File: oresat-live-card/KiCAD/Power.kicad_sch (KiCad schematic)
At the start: 112 parts, among them Q2 PMV45EN2R, Q3 DMP2240UDM, Q4 PMV45EN2R, Q5 DMP3050LVT-7, Q6 DMP3050LVT-7, U12 MIC842LYC5, U13 MIC842LYC5, U14 MAX4211FETE, U15 LTC3624-5, U16 MAX7310ATE, U21 TLV733P-Q1, U22 TS5A21366, U5 LTC3624-5

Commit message: Updated OreSat Live Card. Added changes from the C3 v6 Octavo circuitry and GPS card update. Fixed some GitHub issues. Board layout still in progress.
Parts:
- added C84, C85: CL05B104KO5NNNC, Resistor_SMD:R_0603_1608Metric, symbol Device:C_Small
- added R75: 10k, Resistor_SMD:R_0603_1608Metric, symbol oresat-passives:R-US
- added R95: 1k, Resistor_SMD:R_0603_1608Metric, symbol oresat-passives:R-US
- added TP28, TP31: TEST-POINT, oresat-misc:TestPoint_Pad_D1.0mm, symbol oresat-misc:Test-Point-1mm-round
- D12, D6, D7, D8, D9: symbol oresat-live-card-eagle-import:LED-GREEN0603 -> Device:LED
- Q2, Q4: symbol oresat-live-card-eagle-import:PMV45EN -> Device:Q_NMOS_GSD
- Q3: symbol oresat-live-card-eagle-import:MOSFET-PCH-SOT23-6 -> oresat-transistors:DMP2240UDM-7
- Q5, Q6: footprint oresat-live-card:SOT23-6 -> Package_TO_SOT_SMD:SOT-23-6; symbol oresat-live-card-eagle-import:MOSFET-PCH-SOT23-6 -> oresat-transistors:DMP3050LVT-7
- R20, R22: value 4.7k -> 10k; symbol oresat-live-card-eagle-import:R-US_0603-A -> oresat-passives:R-US
- R32, R33, R34, R35, R36, R37, R38, R39, R40, R41, R42, R43, R44, R45, R46, R47, R48, R49, R50, R51, R52, R53, R54, R55, R56, R57, R58, R59, R60, R61, R62, R64, R65, R66, R67, R68, R69, R70, R71, R72, R94: symbol oresat-live-card-eagle-import:R-US_0603-A -> oresat-passives:R-US
- R63: symbol oresat-live-card-eagle-import:R-US_R1206 -> oresat-passives:R-US
- R92, R93: value 1k -> 100; symbol oresat-live-card-eagle-import:R-US_0603-A -> oresat-passives:R-US
- TP19, TP23, TP24, TP26, TP41, TP42, TP43, TP44, TP45, TP47, TP52, TP53, TP54, TP55, TP57, TP63, TP64, TP67, TP68: footprint oresat-live-card:PAD.03X.04 -> oresat-misc:TestPoint_Pad_D1.0mm; symbol oresat-live-card-eagle-import:TEST-POINT -> oresat-misc:Test-Point-1mm-round
- U12, U13: symbol oresat-live-card-eagle-import:MIC842LYC5 -> oresat-ics:MIC842LYC5
- U14: symbol oresat-live-card-eagle-import:MAX4211 -> oresat-ics:MAX4211FETE
- U15, U5: symbol U-Linear Tech-LTC3624:LTC3624 -> oresat-ics:LTC3624
- U16: symbol oresat-live-card-eagle-import:MAX7310 -> oresat-ics:MAX7310
- U21: symbol U-TI-TLV73311PQDBVRQ1-Linear:TLV733P-Q1 -> oresat-ics:TLV733P-Q1
- U22: symbol U-TI-TS5A21366-2xSPST-analog-switch:TS5A21366 -> oresat-ics:TS5A21366
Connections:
- net CB_CTRL: now also R75.1; no longer Q5.1 (G), R64.1
- net GND: now also D12.1 (K), D6.1 (K), D7.1 (K), D8.1 (K), D9.1 (K), U14.17 (GND), U16.17 (GND); no longer D12.C, D6.C, D7.C, D8.C, D9.C, U14.EPAD (GND), U16.EPAD (GND)
- net VBUS: now also Q6.1 (D), Q6.2 (D), Q6.6 (D)
- net VBUSP: now also Q5.4 (S), C85.1; no longer Q5.6 (D)
- net at Q4.3 (D), R52.1: now also Q6.3 (G); no longer Q6.1 (G)
- net at R20.2: now also D8.2 (A); no longer D8.A
- net at Q5.5 (D), R63.2, R64.2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: now also Q5.1 (D), Q5.2 (D), Q5.6 (D), C84.2
- net at R61.1: now also D7.2 (A); no longer D7.A
- net at C44.1, R63.1, U14.16 (RS+): now also Q6.4 (S); no longer Q6.6 (D)
- net at R49.1: now also D6.2 (A); no longer D6.A
- net at U16.11 (IO6): now also TP31.1
- net at R22.2: now also D9.2 (A); no longer D9.A
- net at R62.2: now also D12.2 (A); no longer D12.A
- net BOOT0: no longer names the net of U16.10 (IO5)
- net BOOT0: now also TP28.1
- net PB6/SCL renamed SYSBOOT2
- net PB7/SDA: no longer names the net of TP68.1, U16.5 (IO1)
- new net: C85.2, R95.1
- new net: C84.1, Q5.3 (G), R64.1, R75.2, R95.2
- no-connect marks 3 -> 2
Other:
- note added: "Circuit breaker switch with ~10 ms soft start"
- note added: "IO0 is open-drain. Pull-up resistor and optional GND jumper on page 4"
- moved on the sheet: C16, C17, C20, C3, C32, C33, C34, C35, C36, C37, C38, C39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

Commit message: Finished layout, and cleaned up more errors/warnings
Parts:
- U15, U5: footprint oresat-footprints:DFN-8-1EP_3x3mm_P0.5mm_EP1.65x2.38mm_ThermalVias0.3mm -> oresat-ics:DFN-8-1EP_3x3mm_P0.5mm_EP1.65x2.38mm_ThermalVias0.3mm
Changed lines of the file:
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@@
       (effects (font (size 1.27 1.27)))
     )
-    (property "Footprint" "oresat-footprints:DFN-8-1EP_3x3mm_P0.5mm_EP1.65x2.38mm_ThermalVias0.3mm" (at 226.06 223.52 0)
+    (property "Footprint" "oresat-ics:DFN-8-1EP_3x3mm_P0.5mm_EP1.65x2.38mm_ThermalVias0.3mm" (at 226.06 223.52 0)
       (effects (font (size 1.27 1.27)) hide)
     )
@@
       (effects (font (size 1.27 1.27)))
     )
-    (property "Footprint" "oresat-footprints:DFN-8-1EP_3x3mm_P0.5mm_EP1.65x2.38mm_ThermalVias0.3mm" (at 344.17 223.52 0)
-      (effects (font (size 1.27 1.27)) hide)
-    )
+    (property "Footprint" "oresat-ics:DFN-8-1EP_3x3mm_P0.5mm_EP1.65x2.38mm_ThermalVias0.3mm" (at 344.17 223.52 0)
+      (effects (font (size 1.27 1.27)) hide)
+    )

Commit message: Updated silk screen and small schematic changes
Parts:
- TP55: footprint oresat-misc:TestPoint_Pad_D1.0mm -> oresat-misc:TestPoint-0.75mm-th
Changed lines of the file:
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@@
       (effects (font (size 1.27 1.27)) hide)
     )
-    (property "Footprint" "oresat-misc:TestPoint_Pad_D1.0mm" (at 407.67 30.48 0)
+    (property "Footprint" "oresat-misc:TestPoint-0.75mm-th" (at 407.67 30.48 0)
       (effects (font (size 1.27 1.27)) hide)
     )

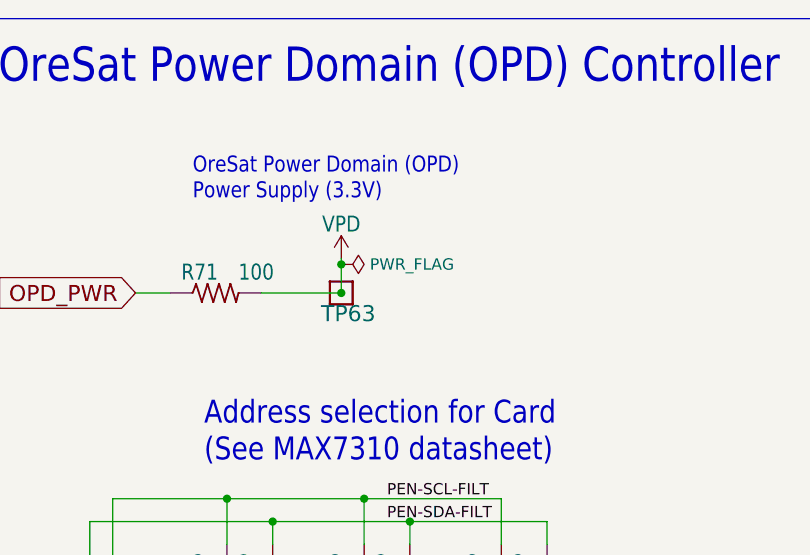
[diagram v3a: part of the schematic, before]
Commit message: Fixed issue with VPD diodes
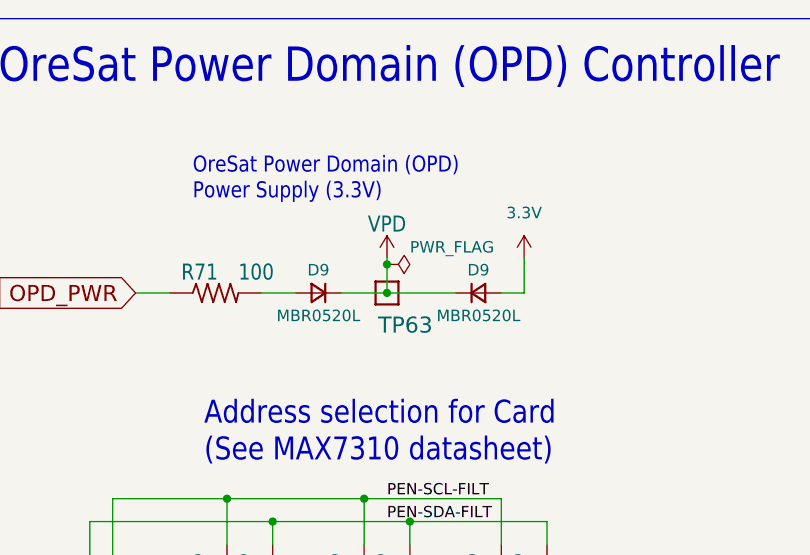
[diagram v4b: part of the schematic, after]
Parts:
- added D9 (x2): MBR0520L, Diode_SMD:D_SOD-123, symbol Device:D_Small
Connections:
- net VPD: now also D9.1 (K), D9.1 (K); no longer R71.2
- new net: D9.2 (A), R71.2
- new net 3.3V: D9.2 (A)
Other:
- moved on the sheet: TP63
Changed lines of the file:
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@@
   (junction (at 266.7 218.44) (diameter 0) (color 0 0 0 0)
   )
-  (junction (at 73.66 48.26) (diameter 0) (color 0 0 0 0)
-  )
   (junction (at 157.48 119.38) (diameter 0) (color 0 0 0 0)
   )
@@
   (junction (at 312.42 218.44) (diameter 0) (color 0 0 0 0)
   )
+  (junction (at 78.74 48.26) (diameter 0) (color 0 0 0 0)
+  )
   (junction (at 368.3 73.66) (diameter 0) (color 0 0 0 0)
   )
@@
   (junction (at 199.39 86.36) (diameter 0) (color 0 0 0 0)
   )
-  (junction (at 73.66 45.085) (diameter 0) (color 0 0 0 0)
+  (junction (at 78.74 45.085) (diameter 0) (color 0 0 0 0)
   )
   (junction (at 321.31 218.44) (diameter 0) (color 0 0 0 0)
@@
     (stroke (width 0) (type default))
   )
+  (wire (pts (xy 73.66 48.26) (xy 78.74 48.26))
+    (stroke (width 0) (type default))
+  )
   (wire (pts (xy 378.46 48.26) (xy 378.46 50.8))
     (stroke (width 0) (type default))
@@
     (stroke (width 0) (type default))
   )
+  (wire (pts (xy 93.98 48.26) (xy 91.44 48.26))
+    (stroke (width 0) (type default))
+  )
   (wire (pts (xy 407.67 35.56) (xy 407.67 40.64))
     (stroke (width 0) (type default))
@@
     (stroke (width 0) (type default))
   )
+  (wire (pts (xy 93.98 44.45) (xy 93.98 48.26))
+    (stroke (width 0) (type default))
+  )
   (wire (pts (xy 311.785 159.385) (xy 311.785 161.925))
     (stroke (width 0) (type default))
@@
     (stroke (width 0) (type default))
   )
-  (wire (pts (xy 73.66 45.085) (xy 73.66 44.45))
+  (wire (pts (xy 78.74 45.085) (xy 78.74 44.45))
     (stroke (width 0) (type default))
   )
@@
     (stroke (width 0) (type default))
   )
+  (wire (pts (xy 78.74 48.26) (xy 86.36 48.26))
+    (stroke (width 0) (type default))
+  )
   (wire (pts (xy 93.98 119.38) (xy 109.22 119.38))
     (stroke (width 0) (type default))
@@
     (stroke (width 0) (type default))
   )
-  (wire (pts (xy 64.77 48.26) (xy 73.66 48.26))
+  (wire (pts (xy 64.77 48.26) (xy 68.58 48.26))
     (stroke (width 0) (type default))
   )
@@
     (stroke (width 0) (type default))
   )
-  (wire (pts (xy 73.66 48.26) (xy 73.66 45.085))
+  (wire (pts (xy 78.74 48.26) (xy 78.74 45.085))
     (stroke (width 0) (type default))
   )
@@
     )
   )
+  (symbol (lib_id "oresat-power:3.3V") (at 93.98 44.45 0) (unit 1)
+    (in_bom yes) (on_board yes) (dnp no) (fields_autoplaced)
+    (property "Reference" "#3V02" (at 93.98 48.26 0)
+      (effects (font (size 1.27 1.27)) hide)
+    )
+    (property "Value" "3.3V" (at 93.98 39.37 0)
+      (effects (font (size 1.27 1.27)))
+    )
+    (property "Footprint" "" (at 93.98 44.45 0)
+      (effects (font (size 1.27 1.27)) hide)
+    )
+    (property "Datasheet" "" (at 93.98 44.45 0)
+      (effects (font (size 1.27 1.27)) hide)
+    )
+    (pin "1")
+    (instances
+      (project "oresat-live-card"
+        (path "/748bdd2d-da0a-4240-ba60-0bf881d2ec56/800b750c-a739-41c9-892a-b7b25d00c873"
+          (reference "#3V02") (unit 1)
+        )
+      )
+    )
+  )
   (symbol (lib_id "Device:R_Small_US") (at 369.57 226.06 90) (unit 1)
     (in_bom yes) (on_board yes) (dnp no)
@@
     )
   )
-  (symbol (lib_id "oresat-power:VPD") (at 73.66 44.45 0) (unit 1)
+  (symbol (lib_id "oresat-power:VPD") (at 78.74 44.45 0) (unit 1)
     (in_bom yes) (on_board yes) (dnp no)
-    (property "Reference" "#VPD01" (at 73.66 44.45 0)
+    (property "Reference" "#VPD01" (at 78.74 44.45 0)
       (effects (font (size 1.27 1.27)) hide)
     )
-    (property "Value" "VPD" (at 73.66 41.656 0)
+    (property "Value" "VPD" (at 78.74 41.656 0)
       (effects (font (size 1.778 1.5113)) (justify bottom))
     )
-    (property "Footprint" "oresat-live-card:" (at 73.66 44.45 0)
+    (property "Footprint" "oresat-live-card:" (at 78.74 44.45 0)
       (effects (font (size 1.27 1.27)) hide)
     )
-    (property "Datasheet" "" (at 73.66 44.45 0)
+    (property "Datasheet" "" (at 78.74 44.45 0)
       (effects (font (size 1.27 1.27)) hide)
     )
@@
     )
   )
+  (symbol (lib_id "Device:D_Small") (at 71.12 48.26 180) (unit 1)
+    (in_bom yes) (on_board yes) (dnp no)
+    (property "Reference" "D9" (at 71.12 45.72 0)
+      (effects (font (size 1.27 1.27)))
+    )
+    (property "Value" "MBR0520L" (at 71.12 50.8 0)
+      (effects (font (size 1.27 1.27)))
+    )
+    (property "Footprint" "Diode_SMD:D_SOD-123" (at 71.12 48.26 90)
+      (effects (font (size 1.27 1.27)) hide)
+    )
+    (property "Datasheet" "~" (at 71.12 48.26 90)
+      (effects (font (size 1.27 1.27)) hide)
+    )
+    (property "Sim.Device" "D" (at 71.12 48.26 0)
+      (effects (font (size 1.27 1.27)) hide)
+    )
+    (property "Sim.Pins" "1=K 2=A" (at 71.12 48.26 0)
+      (effects (font (size 1.27 1.27)) hide)
+    )
+    (pin "1")
+    (pin "2")
+    (instances
+      (project "oresat-gps-card"
+        (path "/65d12cdd-c326-4033-9053-c59fa4e0b25e/0c1da208-2d1c-4d05-9cc7-59584e50a6ac"
+          (reference "D9") (unit 1)
+        )
+      )
+      (project "oresat-live-card"
+        (path "/748bdd2d-da0a-4240-ba60-0bf881d2ec56/7c9c8fbf-83c8-4463-803c-a3967b810f93"
+          (reference "D13") (unit 1)
+        )
+        (path "/748bdd2d-da0a-4240-ba60-0bf881d2ec56/800b750c-a739-41c9-892a-b7b25d00c873"
+          (reference "D13") (unit 1)
+        )
+      )
+    )
+  )
   (symbol (lib_id "oresat-passives:R-US") (at 60.96 91.44 270) (unit 1)
     (in_bom yes) (on_board yes) (dnp no)
@@
     )
   )
-  (symbol (lib_id "oresat-misc:Test-Point-1mm-round") (at 73.66 48.26 180) (unit 1)
+  (symbol (lib_id "oresat-misc:Test-Point-1mm-round") (at 78.74 48.26 180) (unit 1)
     (in_bom yes) (on_board yes) (dnp no)
-    (property "Reference" "TP63" (at 77.47 49.53 0)
+    (property "Reference" "TP63" (at 83.82 50.8 0)
       (effects (font (size 1.778 1.778)) (justify left bottom))
     )
-    (property "Value" "TEST-POINT" (at 73.66 48.26 0)
+    (property "Value" "TEST-POINT" (at 78.74 48.26 0)
       (effects (font (size 1.27 1.27)) hide)
     )
-    (property "Footprint" "oresat-misc:TestPoint_Pad_D1.0mm" (at 73.66 58.42 0)
+    (property "Footprint" "oresat-misc:TestPoint_Pad_D1.0mm" (at 78.74 58.42 0)
       (effects (font (size 1.27 1.27)) hide)
     )
-    (property "Datasheet" "" (at 73.66 48.26 0)
+    (property "Datasheet" "" (at 78.74 48.26 0)
       (effects (font (size 1.27 1.27)) hide)
     )
@@
     )
   )
-  (symbol (lib_id "power:PWR_FLAG") (at 73.66 45.085 270) (unit 1)
-    (in_bom yes) (on_board yes) (dnp no) (fields_autoplaced)
-    (property "Reference" "#FLG02" (at 75.565 45.085 0)
+  (symbol (lib_id "power:PWR_FLAG") (at 78.74 45.085 270) (unit 1)
+    (in_bom yes) (on_board yes) (dnp no)
+    (property "Reference" "#FLG02" (at 80.645 45.085 0)
       (effects (font (size 1.27 1.27)) hide)
     )
-    (property "Value" "PWR_FLAG" (at 76.835 45.085 90)
+    (property "Value" "PWR_FLAG" (at 81.28 43.18 90)
       (effects (font (size 1.27 1.27)) (justify left))
     )
-    (property "Footprint" "" (at 73.66 45.085 0)
+    (property "Footprint" "" (at 78.74 45.085 0)
       (effects (font (size 1.27 1.27)) hide)
     )
-    (property "Datasheet" "~" (at 73.66 45.085 0)
+    (property "Datasheet" "~" (at 78.74 45.085 0)
       (effects (font (size 1.27 1.27)) hide)
     )
@@
         )
       )
+    )
+  )
+  (symbol (lib_id "Device:D_Small") (at 88.9 48.26 0) (unit 1)
+    (in_bom yes) (on_board yes) (dnp no)
+    (property "Reference" "D9" (at 88.9 45.72 0)
+      (effects (font (size 1.27 1.27)))
+    )
+    (property "Value" "MBR0520L" (at 88.9 50.8 0)
+      (effects (font (size 1.27 1.27)))
+    )
+    (property "Footprint" "Diode_SMD:D_SOD-123" (at 88.9 48.26 90)
+      (effects (font (size 1.27 1.27)) hide)
+    )
+    (property "Datasheet" "~" (at 88.9 48.26 90)
+      (effects (font (size 1.27 1.27)) hide)
+    )
+    (property "Sim.Device" "D" (at 88.9 48.26 0)
+      (effects (font (size 1.27 1.27)) hide)
+    )
+    (property "Sim.Pins" "1=K 2=A" (at 88.9 48.26 0)
+      (effects (font (size 1.27 1.27)) hide)
+    )
+    (pin "1")
+    (pin "2")
+    (instances
+      (project "oresat-gps-card"
+        (path "/65d12cdd-c326-4033-9053-c59fa4e0b25e/0c1da208-2d1c-4d05-9cc7-59584e50a6ac"
+          (reference "D9") (unit 1)
+        )
+      )
+      (project "oresat-live-card"
+        (path "/748bdd2d-da0a-4240-ba60-0bf881d2ec56/7c9c8fbf-83c8-4463-803c-a3967b810f93"
+          (reference "D14") (unit 1)
+        )
+        (path "/748bdd2d-da0a-4240-ba60-0bf881d2ec56/800b750c-a739-41c9-892a-b7b25d00c873"
+          (reference "D14") (unit 1)
+        )
+      )

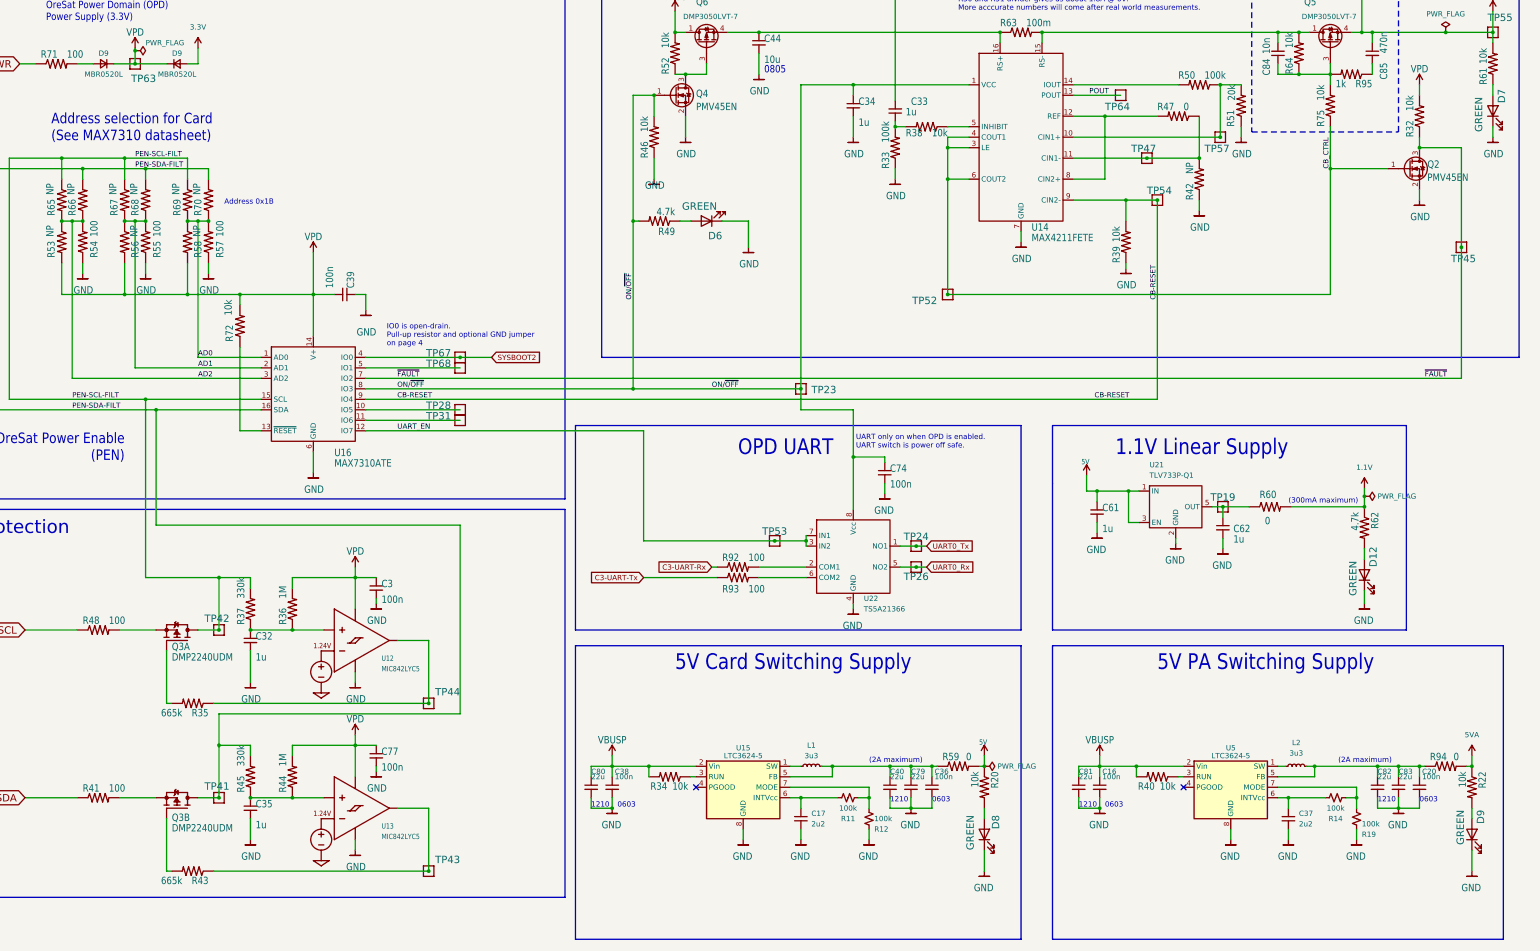
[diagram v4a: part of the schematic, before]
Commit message: Cleaned up ERC and DRC errors on DxWiFi Card
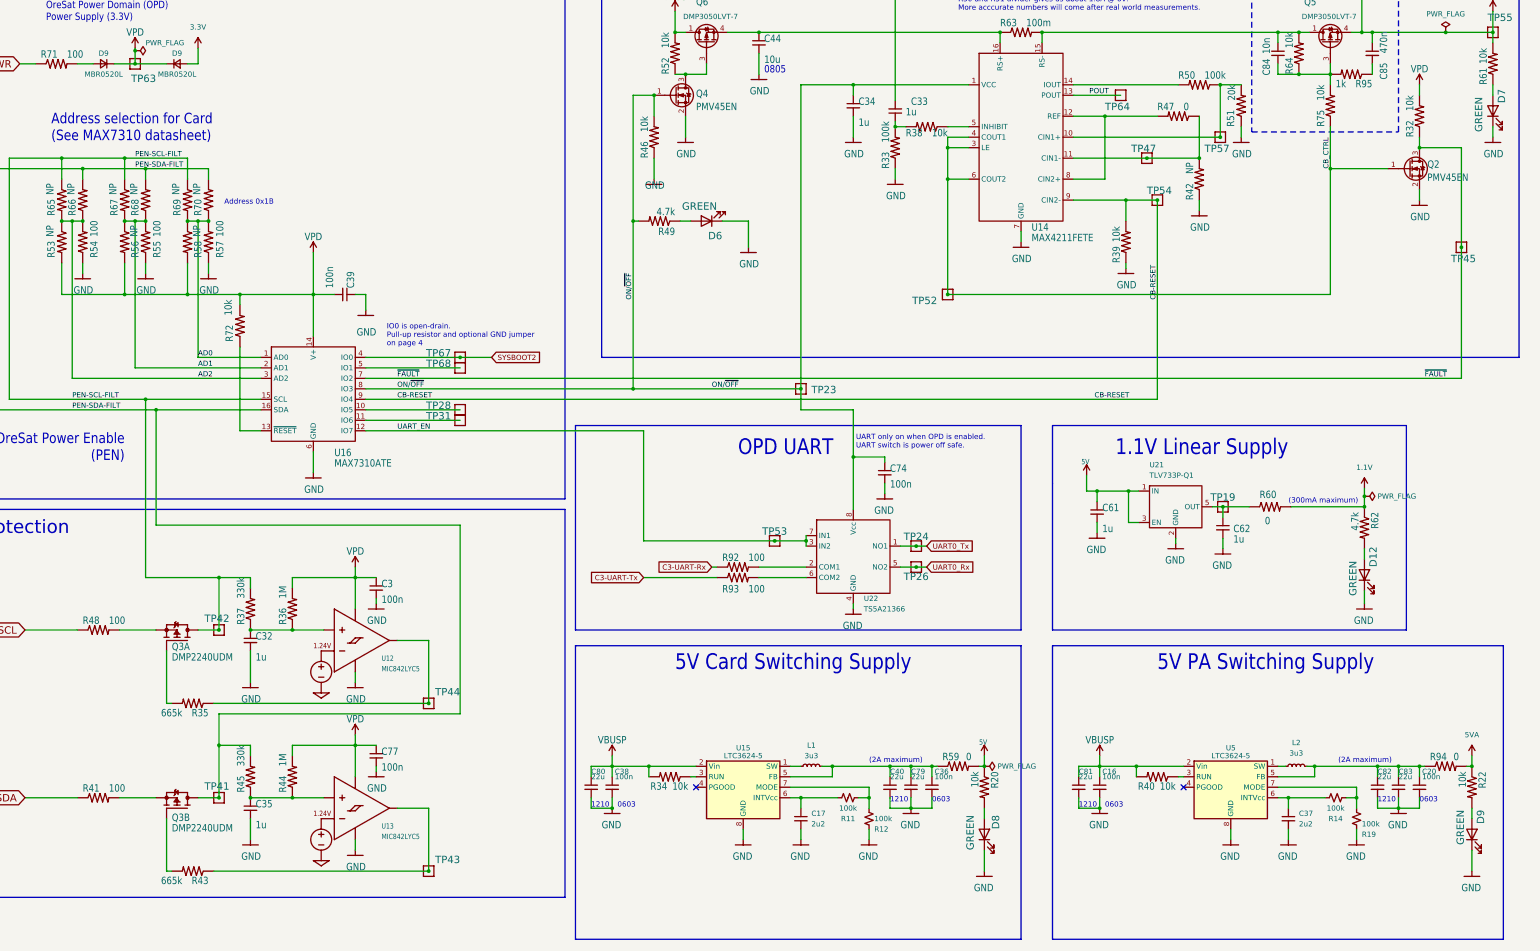
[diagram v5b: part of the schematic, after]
